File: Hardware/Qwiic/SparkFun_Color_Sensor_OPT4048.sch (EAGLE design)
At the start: 29 parts, among them J1 QWIIC_RIGHT_ANGLE, J2 QWIIC_RIGHT_ANGLE, U1 OPT4048

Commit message: Rolls version
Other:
- note added: "v10"
- note removed: "v01"
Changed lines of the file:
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@@
 <wire x1="114.3" y1="185.42" x2="114.3" y2="129.54" width="0.2032" layer="97" style="longdash"/>
 <text x="55.626" y="175.514" size="1.778" layer="97" font="vector" align="center">VDD Range: 1.71V - 3.6V</text>
-<text x="238.76" y="7.62" size="2.54" layer="94" font="vector">v01</text>
+<text x="238.76" y="7.62" size="2.54" layer="94" font="vector">v10</text>
 <text x="177.8" y="180.34" size="2.54" layer="94" font="vector" align="center">Jumpers</text>
 <text x="218.44" y="137.16" size="1.778" layer="97" font="vector">Cut trace to

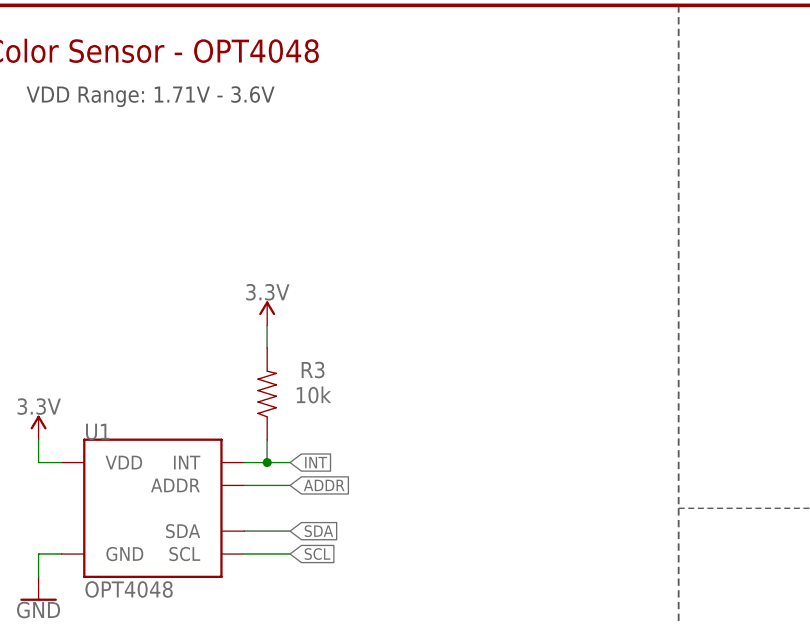
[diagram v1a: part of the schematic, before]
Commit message: Adds jumper to interrupt pin on both designs
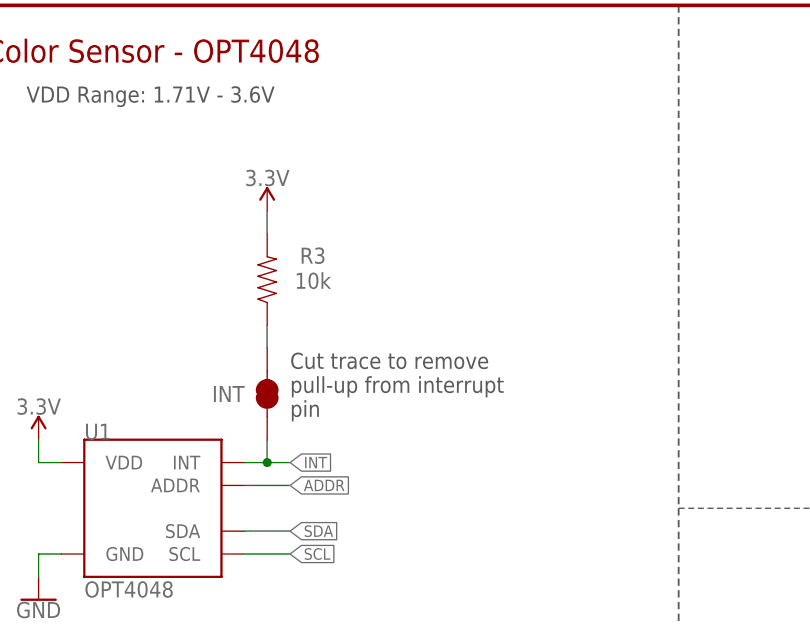
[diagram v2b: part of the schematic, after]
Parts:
- added INT: JUMPER-SMT_2_NC_TRACE_SILK, SparkFun-Jumpers:JUMPER-SMT_2_NC_TRACE_SILK
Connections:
- new net N$1: INT.2, R3.1
- net INT: now also INT.1; no longer R3.1
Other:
- note added: "Cut trace to remove pull-up from interrupt pin"
- moved on the sheet: R3
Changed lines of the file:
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@@
 <part name="0X45" library="SparkFun-Jumpers" deviceset="JUMPER-SMT_2_NO" device="_SILK" package3d_urn="urn:adsk.eagle:package:39279/1"/>
 <part name="0X44" library="SparkFun-Jumpers" deviceset="JUMPER-SMT_2_NC_TRACE" device="_SILK" package3d_urn="urn:adsk.eagle:package:39281/1"/>
+<part name="INT" library="SparkFun-Jumpers" deviceset="JUMPER-SMT_2_NC_TRACE" device="_SILK" package3d_urn="urn:adsk.eagle:package:39281/1"/>
 </parts>
 <sheets>
@@
 <text x="177.8" y="116.84" size="1.778" layer="97" font="vector" align="center">Close Jumper to select
 Address</text>
+<text x="71.12" y="139.7" size="1.778" layer="97" font="vector">Cut trace to remove
+pull-up from interrupt
+pin</text>
 </plain>
 <instances>
@@
 <attribute name="VALUE" x="43.18" y="119.126" size="1.778" layer="96" font="vector" align="top-center"/>
 </instance>
-<instance part="R3" gate="G$1" x="68.58" y="142.24" smashed="yes" rot="R90">
-<attribute name="NAME" x="73.66" y="145.796" size="1.778" layer="95" font="vector" rot="R180" align="bottom-center"/>
-<attribute name="VALUE" x="73.66" y="141.224" size="1.778" layer="96" font="vector" rot="R180" align="top-center"/>
-</instance>
-<instance part="SUPPLY7" gate="G$1" x="68.58" y="149.86" smashed="yes">
-<attribute name="VALUE" x="68.58" y="152.654" size="1.778" layer="96" font="vector" align="bottom-center"/>
+<instance part="R3" gate="G$1" x="68.58" y="154.94" smashed="yes" rot="R90">
+<attribute name="NAME" x="73.66" y="158.496" size="1.778" layer="95" font="vector" rot="R180" align="bottom-center"/>
+<attribute name="VALUE" x="73.66" y="153.924" size="1.778" layer="96" font="vector" rot="R180" align="top-center"/>
+</instance>
+<instance part="SUPPLY7" gate="G$1" x="68.58" y="162.56" smashed="yes">
+<attribute name="VALUE" x="68.58" y="165.354" size="1.778" layer="96" font="vector" align="bottom-center"/>
 </instance>
 <instance part="SUPPLY8" gate="G$1" x="142.24" y="119.38" smashed="yes">
@@
 <instance part="0X44" gate="G$1" x="134.62" y="88.9" smashed="yes">
 <attribute name="NAME" x="134.62" y="91.694" size="1.778" layer="95" font="vector" align="center"/>
+</instance>
+<instance part="INT" gate="G$1" x="68.58" y="142.24" smashed="yes" rot="R90">
+<attribute name="NAME" x="64.262" y="142.24" size="1.778" layer="95" font="vector" rot="R180" align="center"/>
 </instance>
 </instances>
@@
 <segment>
 <pinref part="U1" gate="G$1" pin="INT"/>
-<wire x1="68.58" y1="134.62" x2="66.04" y2="134.62" width="0.1524" layer="91"/>
+<label x="71.12" y="134.62" size="1.27" layer="95" font="vector" xref="yes"/>
+<wire x1="66.04" y1="134.62" x2="68.58" y2="134.62" width="0.1524" layer="91"/>
+<pinref part="INT" gate="G$1" pin="1"/>
+<wire x1="68.58" y1="134.62" x2="71.12" y2="134.62" width="0.1524" layer="91"/>
 <wire x1="68.58" y1="137.16" x2="68.58" y2="134.62" width="0.1524" layer="91"/>
-<pinref part="R3" gate="G$1" pin="1"/>
-<label x="71.12" y="134.62" size="1.27" layer="95" font="vector" xref="yes"/>
-<wire x1="68.58" y1="134.62" x2="71.12" y2="134.62" width="0.1524" layer="91"/>
 <junction x="68.58" y="134.62"/>
 </segment>
@@
 <segment>
 <pinref part="R3" gate="G$1" pin="2"/>
-<wire x1="68.58" y1="149.86" x2="68.58" y2="147.32" width="0.1524" layer="91"/>
+<wire x1="68.58" y1="162.56" x2="68.58" y2="160.02" width="0.1524" layer="91"/>
 <pinref part="SUPPLY7" gate="G$1" pin="3.3V"/>
 </segment>
@@
 </segment>
 </net>
+<net name="N$1" class="0">
+<segment>
+<pinref part="INT" gate="G$1" pin="2"/>
+<pinref part="R3" gate="G$1" pin="1"/>
+<wire x1="68.58" y1="147.32" x2="68.58" y2="149.86" width="0.1524" layer="91"/>
+</segment>
+</net>

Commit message: Revert "Adds jumper to interrupt pin on both designs"
This reverts commit a39334068ad88ec2875ce3e39fad74091b9d5839.
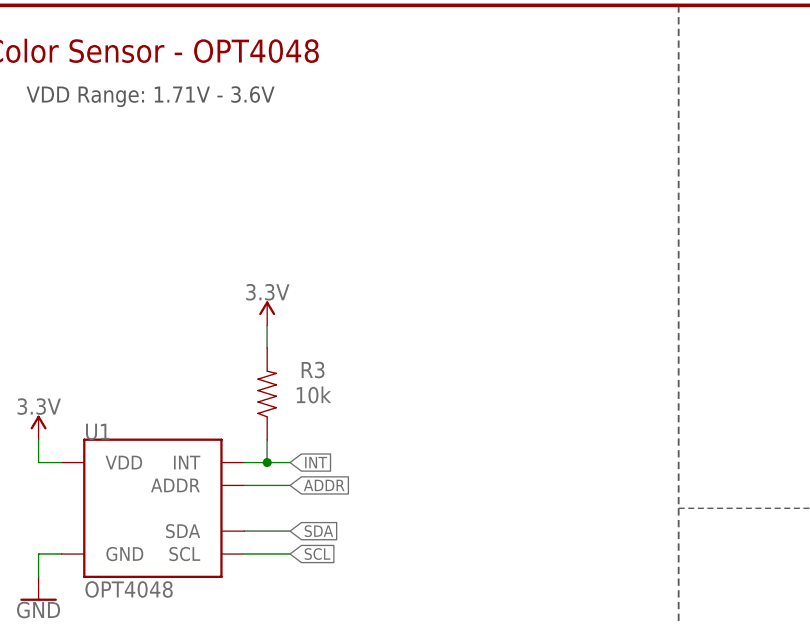
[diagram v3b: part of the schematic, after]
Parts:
- removed INT: JUMPER-SMT_2_NC_TRACE_SILK, SparkFun-Jumpers:JUMPER-SMT_2_NC_TRACE_SILK
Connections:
- removed net N$1: INT.2, R3.1
- net INT: now also R3.1; no longer INT.1
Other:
- note removed: "Cut trace to remove pull-up from interrupt pin"
- moved on the sheet: R3
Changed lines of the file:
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@@
 <part name="0X45" library="SparkFun-Jumpers" deviceset="JUMPER-SMT_2_NO" device="_SILK" package3d_urn="urn:adsk.eagle:package:39279/1"/>
 <part name="0X44" library="SparkFun-Jumpers" deviceset="JUMPER-SMT_2_NC_TRACE" device="_SILK" package3d_urn="urn:adsk.eagle:package:39281/1"/>
-<part name="INT" library="SparkFun-Jumpers" deviceset="JUMPER-SMT_2_NC_TRACE" device="_SILK" package3d_urn="urn:adsk.eagle:package:39281/1"/>
 </parts>
 <sheets>
@@
 <text x="177.8" y="116.84" size="1.778" layer="97" font="vector" align="center">Close Jumper to select
 Address</text>
-<text x="71.12" y="139.7" size="1.778" layer="97" font="vector">Cut trace to remove
-pull-up from interrupt
-pin</text>
 </plain>
 <instances>
@@
 <attribute name="VALUE" x="43.18" y="119.126" size="1.778" layer="96" font="vector" align="top-center"/>
 </instance>
-<instance part="R3" gate="G$1" x="68.58" y="154.94" smashed="yes" rot="R90">
-<attribute name="NAME" x="73.66" y="158.496" size="1.778" layer="95" font="vector" rot="R180" align="bottom-center"/>
-<attribute name="VALUE" x="73.66" y="153.924" size="1.778" layer="96" font="vector" rot="R180" align="top-center"/>
-</instance>
-<instance part="SUPPLY7" gate="G$1" x="68.58" y="162.56" smashed="yes">
-<attribute name="VALUE" x="68.58" y="165.354" size="1.778" layer="96" font="vector" align="bottom-center"/>
+<instance part="R3" gate="G$1" x="68.58" y="142.24" smashed="yes" rot="R90">
+<attribute name="NAME" x="73.66" y="145.796" size="1.778" layer="95" font="vector" rot="R180" align="bottom-center"/>
+<attribute name="VALUE" x="73.66" y="141.224" size="1.778" layer="96" font="vector" rot="R180" align="top-center"/>
+</instance>
+<instance part="SUPPLY7" gate="G$1" x="68.58" y="149.86" smashed="yes">
+<attribute name="VALUE" x="68.58" y="152.654" size="1.778" layer="96" font="vector" align="bottom-center"/>
 </instance>
 <instance part="SUPPLY8" gate="G$1" x="142.24" y="119.38" smashed="yes">
@@
 <instance part="0X44" gate="G$1" x="134.62" y="88.9" smashed="yes">
 <attribute name="NAME" x="134.62" y="91.694" size="1.778" layer="95" font="vector" align="center"/>
-</instance>
-<instance part="INT" gate="G$1" x="68.58" y="142.24" smashed="yes" rot="R90">
-<attribute name="NAME" x="64.262" y="142.24" size="1.778" layer="95" font="vector" rot="R180" align="center"/>
 </instance>
 </instances>
@@
 <segment>
 <pinref part="U1" gate="G$1" pin="INT"/>
+<wire x1="68.58" y1="134.62" x2="66.04" y2="134.62" width="0.1524" layer="91"/>
+<wire x1="68.58" y1="137.16" x2="68.58" y2="134.62" width="0.1524" layer="91"/>
+<pinref part="R3" gate="G$1" pin="1"/>
 <label x="71.12" y="134.62" size="1.27" layer="95" font="vector" xref="yes"/>
-<wire x1="66.04" y1="134.62" x2="68.58" y2="134.62" width="0.1524" layer="91"/>
-<pinref part="INT" gate="G$1" pin="1"/>
 <wire x1="68.58" y1="134.62" x2="71.12" y2="134.62" width="0.1524" layer="91"/>
-<wire x1="68.58" y1="137.16" x2="68.58" y2="134.62" width="0.1524" layer="91"/>
 <junction x="68.58" y="134.62"/>
 </segment>
@@
 <segment>
 <pinref part="R3" gate="G$1" pin="2"/>
-<wire x1="68.58" y1="162.56" x2="68.58" y2="160.02" width="0.1524" layer="91"/>
+<wire x1="68.58" y1="149.86" x2="68.58" y2="147.32" width="0.1524" layer="91"/>
 <pinref part="SUPPLY7" gate="G$1" pin="3.3V"/>
 </segment>
@@
 </segment>
 </net>
-<net name="N$1" class="0">
-<segment>
-<pinref part="INT" gate="G$1" pin="2"/>
-<pinref part="R3" gate="G$1" pin="1"/>
-<wire x1="68.58" y1="147.32" x2="68.58" y2="149.86" width="0.1524" layer="91"/>
-</segment>
-</net>
